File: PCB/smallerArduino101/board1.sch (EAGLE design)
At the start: 41 parts

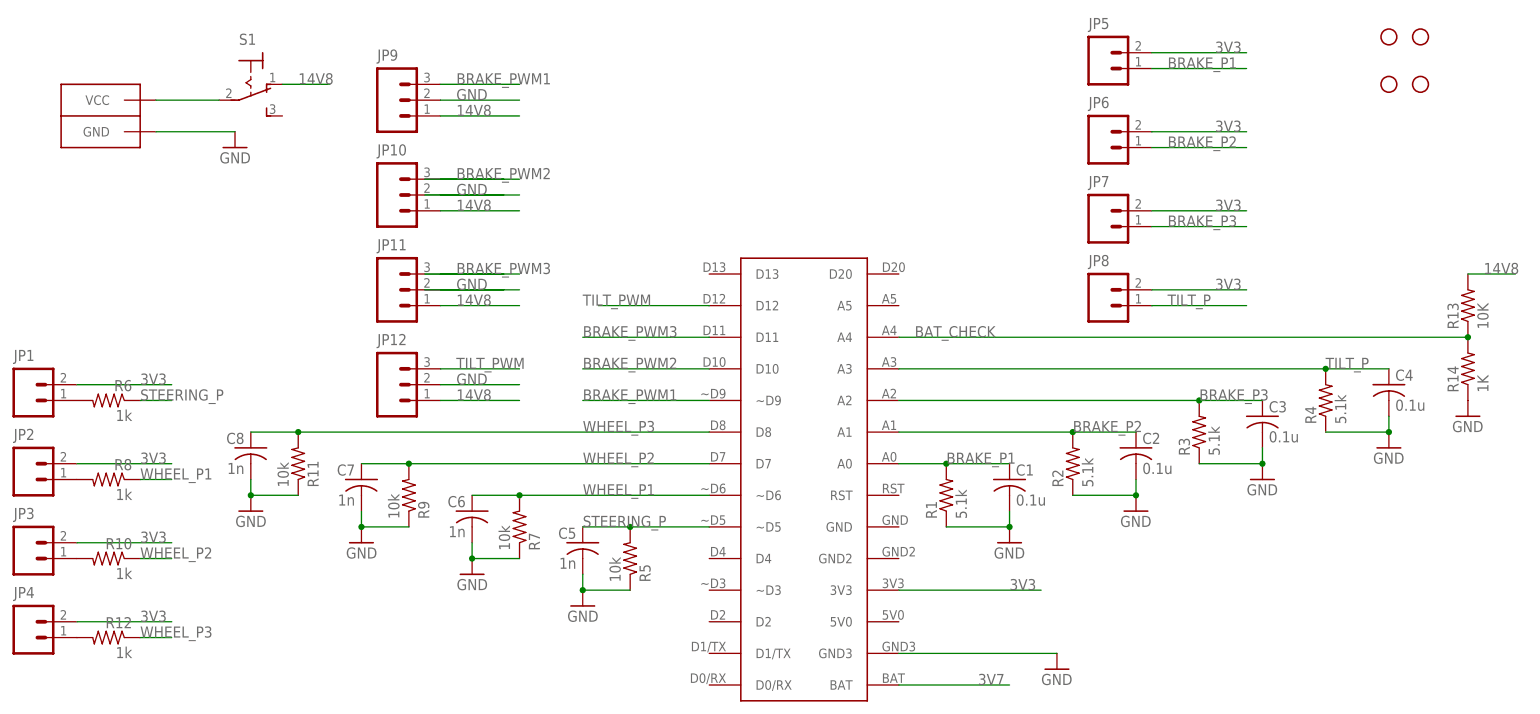
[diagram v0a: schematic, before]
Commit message: renamed jumpers and connectors
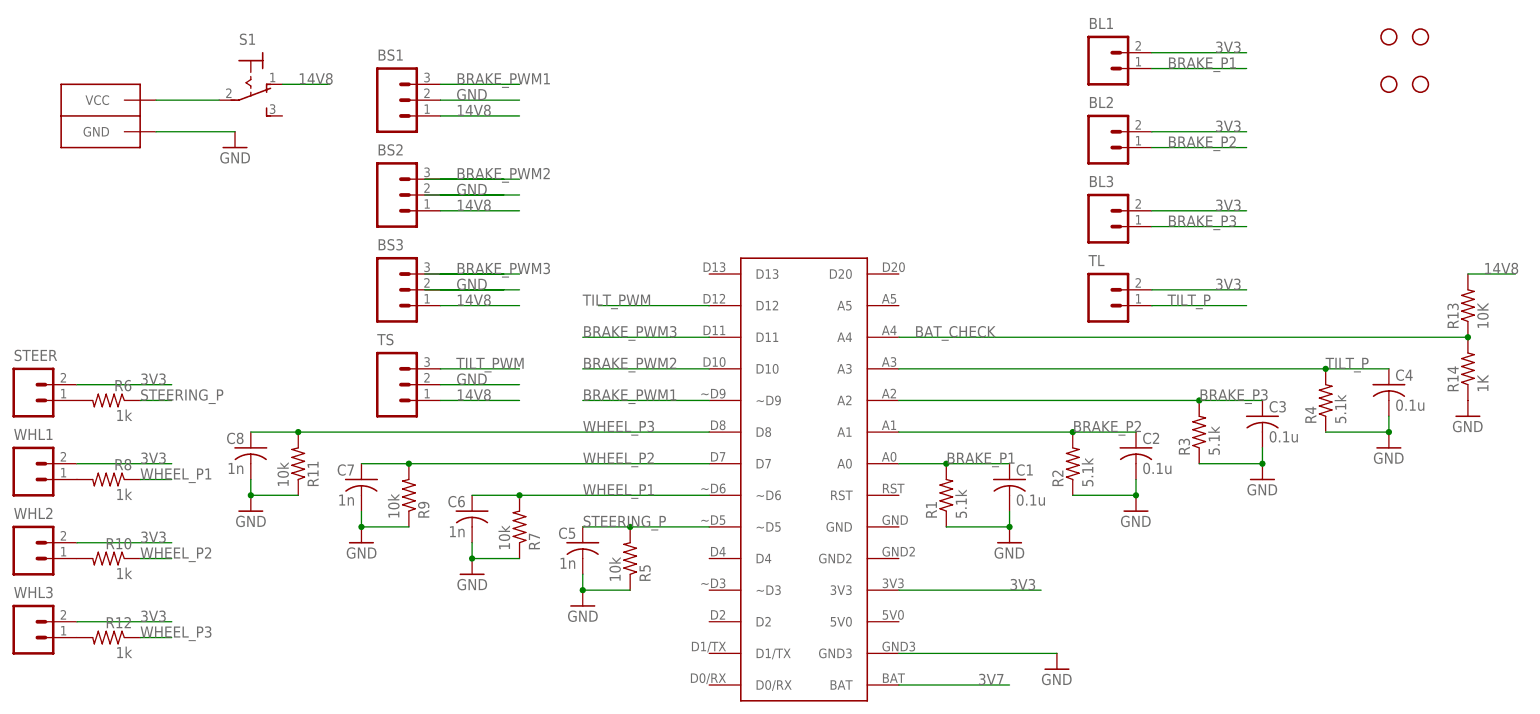
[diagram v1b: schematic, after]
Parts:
- renumbered CONN1 to 14V8, JP1 to STEER, JP10 to BS2, JP11 to BS3, JP12 to TS, JP2 to WHL1, JP3 to WHL2, JP4 to WHL3, JP5 to BL1, JP6 to BL2, JP7 to BL3, JP8 to TL, JP9 to BS1
